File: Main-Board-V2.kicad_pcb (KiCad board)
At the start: 4 copper layers, 350 x 60 mm, 58 parts, among them IC1 REG1117-5, J2 776280-1, J3 776280-1, J4 1-776231-4, K1 J107F1AS123VDC.36, K2 J107F1AS123VDC.36, K3 J107F1AS123VDC.36, Q1 2N2222A, Q2 2N2222A, Q3 2N2222A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

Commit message: Moved CAN Ports to same side of board
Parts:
- moved C3 234.4 mm to (333.0, 105.7), turned to 180 degrees
- moved IC1 228.1 mm to (332.0, 112.0), turned to -90 degrees
- moved C2 224.5 mm to (326.1, 112.3)
- moved J3 69.8 mm to (130.8, 70.3), turned to 180 degrees
- moved U2 35.4 mm to (102.5, 97.0)
- moved C9 20.0 mm to (72.3, 110.1), turned to 180 degrees
- moved U3 19.9 mm to (71.5, 88.0), turned to 90 degrees
- moved C8 19.4 mm to (78.4, 102.4), turned to 90 degrees
- moved C4 18.0 mm to (71.6, 93.1), turned to 180 degrees
- moved C5 14.1 mm to (77.4, 85.7), turned to 90 degrees
- moved U12 11.2 mm to (72.5, 105.0), turned to 90 degrees
- moved J2 0.19 mm to (74.5, 70.3)
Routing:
- net /Can_RX1: track 108.6 -> 37.1 mm, vias 1 -> 0
- net /Can_TX1: track 128.5 -> 63.0 mm, vias 1 -> 0
- net +5V: track 361.7 -> 416.1 mm, vias 4 -> 2
- net +12V: track 291.9 -> 250.2 mm, vias 0 -> 2
- net /BattRelay: track 198.3 -> 233.1 mm
- net /USART_RX: track 116.8 -> 151.6 mm
- net /RightSignalIO: track 167.9 -> 202.7 mm
- net /Pedal/ThrottleIO: track 158.3 -> 193.1 mm
- net /Dio5: track 91.6 -> 126.4 mm
- net /Dio2: track 59.3 -> 94.1 mm
- net /ErrorIO: track 32.2 -> 67.0 mm
- net /Dio3: track 46.6 -> 81.4 mm
- net /USART_TX: track 119.4 -> 154.2 mm
- net /Pedal/BrakeIO: track 135.3 -> 170.1 mm
- net /LeftSignalIO: track 182.9 -> 217.7 mm
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
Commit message: Finalized analog components. Everything is done 🙏
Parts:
- removed R28, R29: R_US, Resistor_SMD:R_0805_2012Metric
- added C1: 1N, Capacitor_SMD:C_0805_2012Metric, F.Cu at (239.3, 107.1)
- added C6: 1N, Capacitor_SMD:C_0805_2012Metric, F.Cu at (255.0, 107.4)
- added C7: 1N, Capacitor_SMD:C_0805_2012Metric, F.Cu at (273.4, 109.5)
- added R6: 100R, Resistor_SMD:R_0805_2012Metric, F.Cu at (271.4, 98.3)
- added R7: 10k, Resistor_SMD:R_0805_2012Metric, F.Cu at (277.5, 99.3)
- C2, C3: footprint Cap10U:CAPC2012X145N -> Capacitor_SMD:C_0805_2012Metric
- R1, R20: value R_US -> 100R
- R2, R21, R22, R23, R24, R26, R3, R4: value R_US -> 10k
- R25, R27, R5: value R_US -> 1k
- moved R27 25.9 mm to (249.4, 107.4), turned to 0 degrees
- moved R25 11.6 mm to (268.8, 108.5)
- moved R26 9.57 mm to (249.4, 102.3), turned to 0 degrees
- moved R23 9.51 mm to (266.8, 103.4), turned to 0 degrees
- moved R22 9.38 mm to (260.6, 98.8), turned to -90 degrees
- moved R1 7.23 mm to (237.2, 96.9), turned to -90 degrees
- moved R3 6.90 mm to (243.3, 103.0)
- moved R21 6.73 mm to (277.5, 104.9), turned to 180 degrees
- moved R4 6.56 mm to (233.2, 102.0), turned to 0 degrees
- moved R2 6.34 mm to (243.8, 97.9), turned to -90 degrees
- moved U1 5.51 mm to (238.2, 101.5), turned to 90 degrees
- moved R20 4.62 mm to (254.0, 97.3), turned to -90 degrees
- moved R24 3.18 mm to (260.6, 103.9)
- moved U10 3.03 mm to (255.0, 102.3), turned to 90 degrees
- moved C3 2.93 mm to (334.4, 103.1)
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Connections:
- R21 pad 1: /Pedal/Throttle+ -> GND
- R21 pad 2: GND -> Net-(U11-+IN)
- R23 pad 1: /Pedal/Throttle+ -> GND
- R23 pad 2: Net-(U11-+IN) -> Net-(U11-OUT)
- R25 pad 1: GND -> Net-(U11-OUT)
- R25 pad 2: Net-(U11-+IN) -> /Pedal/ThrottleIO
- R27 pad 1: GND -> Net-(U10-OUT)
- R27 pad 2: Net-(U11-OUT) -> /Pedal/BrakeIO
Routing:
- net +12V: track 250.2 -> 277.5 mm, vias 2 -> 1
- net /EncoderIO: track 141.6 -> 151.5 mm
- net /Pedal/Brake+: track 33.6 -> 26.7 mm
- net /Pedal/ThrottleIO: track 193.1 -> 188.1 mm
- net /Encoder: track 30.8 -> 25.9 mm
- net Net-(U10-OUT): track 5.20 -> 10.1 mm
- net GND: track 142.3 -> 139.5 mm, vias 20 -> 15
- net Net-(U11-OUT): track 6.29 -> 8.81 mm
- net Net-(U11-+IN): track 6.39 -> 8.89 mm
- net /Pedal/BrakeIO: track 170.1 -> 168.0 mm
- net Net-(U10-+IN): track 6.30 -> 8.38 mm
- net +5V: track 416.1 -> 414.4 mm
- net +3.3V: track 217.2 -> 218.8 mm, vias 4 -> 8
- net Net-(U1-OUT): track 8.80 -> 9.93 mm
- net /Pedal/Throttle+: track 34.2 -> 33.5 mm
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
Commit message: Added fuse, switch to horizontal connecotor, redid all routing
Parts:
- added F1: Fuse, Fuse:Fuse_0805_2012Metric, F.Cu at (187.5, 81.5)
- J4: value 1-776231-4 -> 1-776163-5; footprint 1-776231-4:TE_1-776231-4 -> 776163-5:TE_776163-5
- moved K2 258.1 mm to (57.5, 98.0)
- moved Q2 258.1 mm to (57.5, 110.7)
- moved R30 258.1 mm to (58.1, 85.3)
- moved K1 244.7 mm to (85.5, 98.0)
- moved Q1 244.7 mm to (85.9, 110.8)
- moved K3 229.1 mm to (71.9, 98.0)
- moved Q3 229.1 mm to (71.9, 110.7)
- moved R31 229.1 mm to (71.3, 85.9)
- moved R7 176.8 mm to (101.0, 111.1)
- moved R6 175.3 mm to (96.5, 111.1)
- moved R21 171.6 mm to (106.0, 111.1), turned to -90 degrees
- moved U11 170.4 mm to (102.0, 117.1), turned to -90 degrees
- moved R23 159.8 mm to (107.5, 116.6), turned to 90 degrees
- moved R25 156.5 mm to (112.5, 116.6), turned to -90 degrees
- moved C7 156.0 mm to (117.5, 116.6)
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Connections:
- J2 pad 1: +12V -> Net-(F1-Pad1)
- J3 pad 1: +12V -> Net-(F1-Pad1)
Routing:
- net +5V: track 414.4 -> 212.5 mm, vias 2 -> 3
- net /Pedal/ThrottleIO: track 188.1 -> 5.02 mm, vias 1 -> 0
- net /Pedal/BrakeIO: track 168.0 -> 4.76 mm, vias 1 -> 0
- net /USART_TX: track 154.2 -> 0.00 mm
- net /USART_RX: track 151.6 -> 0.00 mm
- net /EncoderIO: track 151.5 -> 0.00 mm, vias 1 -> 0
- net /BattRelay: track 233.1 -> 93.7 mm
- net /RightSignalIO: track 202.4 -> 108.1 mm
- net /LeftSignalIO: track 217.7 -> 123.9 mm
- net /Pedal/Error: track 95.9 -> 12.3 mm
- net /Dio1: track 106.5 -> 32.2 mm
- net /Dio4: track 116.0 -> 50.5 mm
- net GND: track 139.5 -> 74.1 mm, vias 15 -> 8
- net /Dio5: track 126.4 -> 69.4 mm
- net /DigitalInputs/Button3: track 73.7 -> 17.5 mm
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- removed copper zone on In2.Cu, net +12V
- removed copper zone on In2.Cu, net +3.3V
- removed copper zone on B.Cu, net GND
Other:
- board size 350 x 60 mm -> 201 x 70.1 mm
- copper layers 4 -> 2

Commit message: finished re-routing, only silkscreen errors left
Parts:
- moved R3 71.6 mm to (143.5, 117.5), turned to 0 degrees
- moved R2 66.8 mm to (143.5, 112.5)
- moved U1 64.7 mm to (148.5, 113.0), turned to -90 degrees
- moved R1 62.6 mm to (143.5, 108.0), turned to 0 degrees
- moved R4 62.2 mm to (153.0, 117.0), turned to 180 degrees
- moved G*** 57.8 mm to (142.0, 96.5)
- moved R5 57.0 mm to (153.0, 112.5), turned to 0 degrees
- moved C1 53.5 mm to (153.0, 108.0), turned to 180 degrees
- moved R21 12.3 mm to (95.5, 117.5), turned to 0 degrees
- moved C7 11.6 mm to (106.0, 117.5), turned to 180 degrees
- moved R24 11.0 mm to (114.0, 117.5), turned to 0 degrees
- moved R20 8.73 mm to (114.0, 108.5), turned to 0 degrees
- moved U10 8.73 mm to (119.5, 113.0)
- moved R26 8.38 mm to (124.5, 108.5), turned to 180 degrees
- moved R23 8.23 mm to (106.0, 108.5), turned to 180 degrees
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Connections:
- C6 pad 1: /Pedal/BrakeIO -> /BrakeIO
- C7 pad 1: /Pedal/ThrottleIO -> /ThrottleIO
- R25 pad 2: /Pedal/ThrottleIO -> /ThrottleIO
- R27 pad 2: /Pedal/BrakeIO -> /BrakeIO
- U2 pad 10: /Dio2 -> unconnected-(U2-8_TX2_IN1-Pad10)
- U2 pad 11: /Dio3 -> unconnected-(U2-9_OUT1C-Pad11)
- U2 pad 12: /ErrorIO -> /BattRelay
- U2 pad 13: unconnected-(U2-11_MOSI_CTX1-Pad13) -> /RightSignalIO
- U2 pad 14: unconnected-(U2-12_MISO_MQSL-Pad14) -> /LeftSignalIO
- U2 pad 23: /USART_RX -> /ThrottleIO
- U2 pad 24: /USART_TX -> /BrakeIO
- U2 pad 25: unconnected-(U2-18_A4_SDA0-Pad25) -> /EncoderIO
- U2 pad 26: /EncoderIO -> unconnected-(U2-19_A5_SCL0-Pad26)
- U2 pad 27: /Pedal/BrakeIO -> /USART_TX
- U2 pad 28: /Pedal/ThrottleIO -> /USART_RX
- U2 pad 4: /BattRelay -> /Dio1
- U2 pad 5: /LeftSignalIO -> /Dio2
- U2 pad 6: /RightSignalIO -> /Dio3
- U2 pad 7: /Dio5 -> /Dio4
- U2 pad 8: /Dio4 -> /Dio5
- U2 pad 9: /Dio1 -> /ErrorIO
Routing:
- net /USART_TX: track 0.00 -> 106.2 mm, vias 0 -> 1
- net /USART_RX: track 0.00 -> 97.8 mm, vias 0 -> 1
- net /ThrottleIO: track 0.00 -> 91.6 mm, vias 0 -> 1
- net /BrakeIO: track 0.00 -> 73.0 mm, vias 0 -> 1
- net /Encoder: track 0.00 -> 72.0 mm
- net +3.3V: track 198.9 -> 257.8 mm, vias 7 -> 9
- net /Pedal/Brake+: track 48.8 -> 4.50 mm
- net /EncoderIO: track 0.00 -> 42.7 mm, vias 0 -> 1
- net GND: track 74.1 -> 111.6 mm, vias 8 -> 16
- net /Pedal/Throttle+: track 37.1 -> 4.50 mm
- net /Dio4: track 50.5 -> 60.1 mm, vias 0 -> 1
- net Net-(U1-+IN): track 0.00 -> 8.45 mm
- net Net-(U1-OUT): track 0.00 -> 7.45 mm
- net /Pedal/ThrottleIO: track 5.02 -> 0.00 mm
- net /Pedal/BrakeIO: track 4.76 -> 0.00 mm
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- added copper zone on B.Cu, net GND
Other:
- board text added: "${REFERENCE}"
- board text removed: "1"
- board text removed: "10"
- board text removed: "11"
- board text removed: "12"
- board text removed: "13"
- board text removed: "14"
- board text removed: "15"
- board text removed: "16"
- board text removed: "17"
- board text removed: "18"
- board text removed: "19"
- board text removed: "2"
- board text removed: "20"
- board text removed: "21"
- board text removed: "22"
- board text removed: "23"
- board text removed: "24"
- board text removed: "25"
- board text removed: "26"
- board text removed: "27"
- board text removed: "28"
- board text removed: "29"
- board text removed: "3"
- board text removed: "30"
- board text removed: "31"
- board text removed: "32"
- board text removed: "33"
- board text removed: "34"
- board text removed: "4"
- board text removed: "5"
- board text removed: "6"
- board text removed: "7"
- board text removed: "8"
- board text removed: "9"

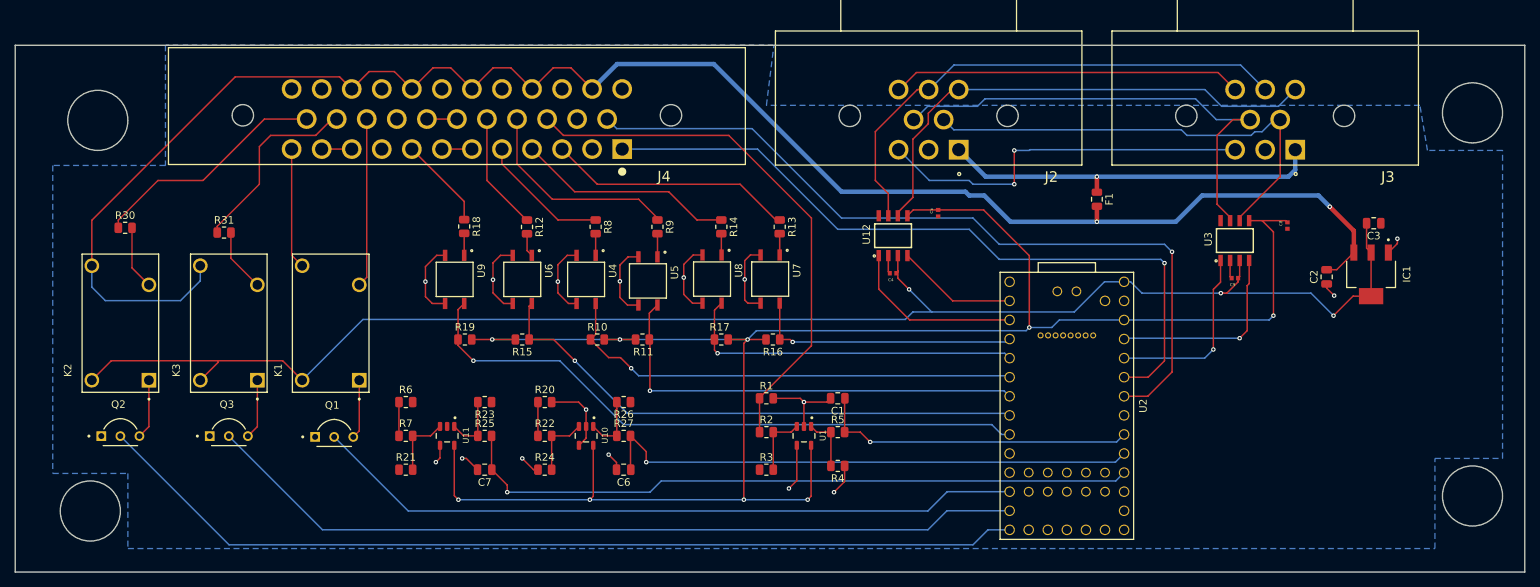
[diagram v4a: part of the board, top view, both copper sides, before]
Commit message: fixed silk screen
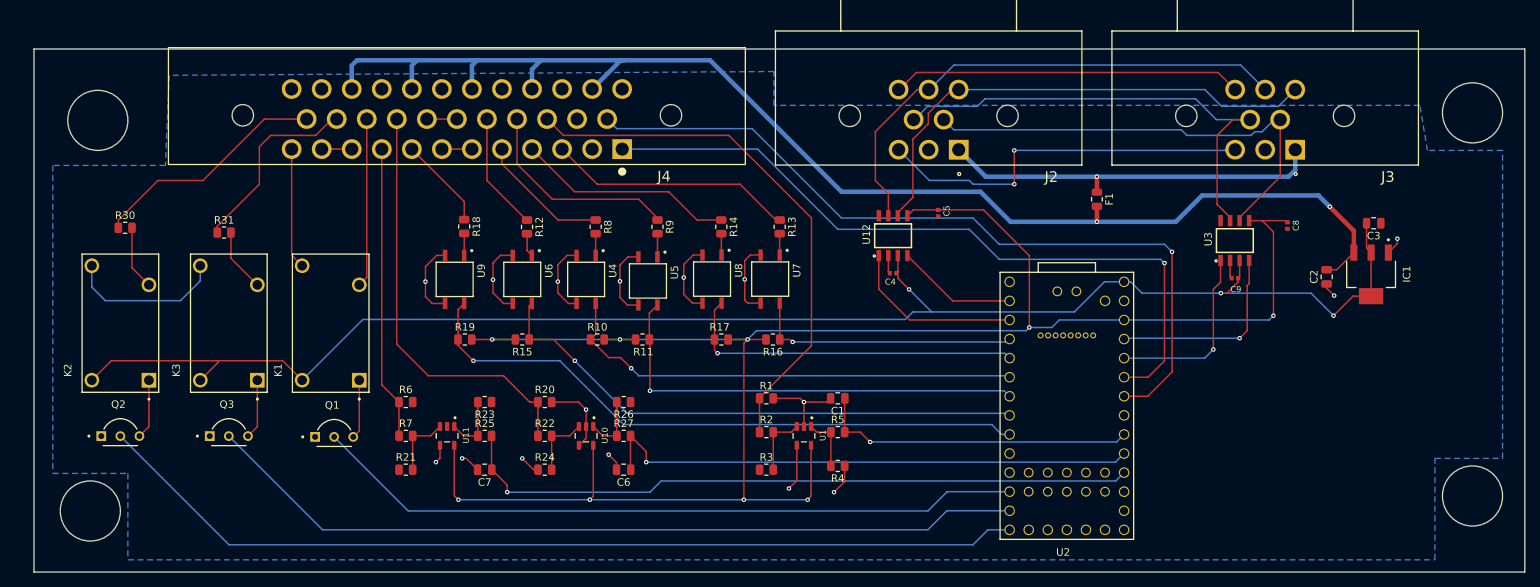
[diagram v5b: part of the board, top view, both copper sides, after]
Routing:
- net /Pedal/Brake+: track 4.50 -> 56.5 mm
- net +12V: track 235.7 -> 198.1 mm
- net /Pedal/Throttle+: track 4.50 -> 39.1 mm
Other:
- board size 201 x 70.1 mm -> 198.5 x 69.6 mm
- board text added: "Teensy4.0"
- board text removed: "${REFERENCE}"

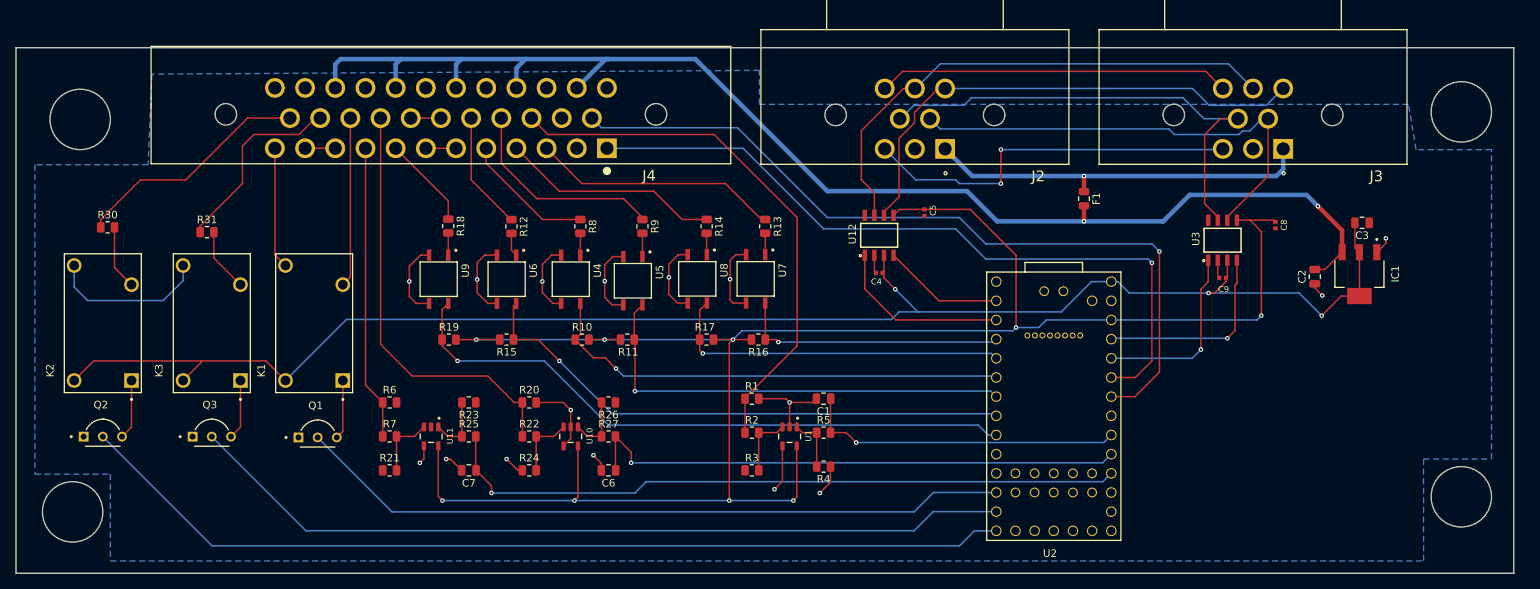
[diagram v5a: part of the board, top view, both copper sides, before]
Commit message: added LED indicators, fixed footprints
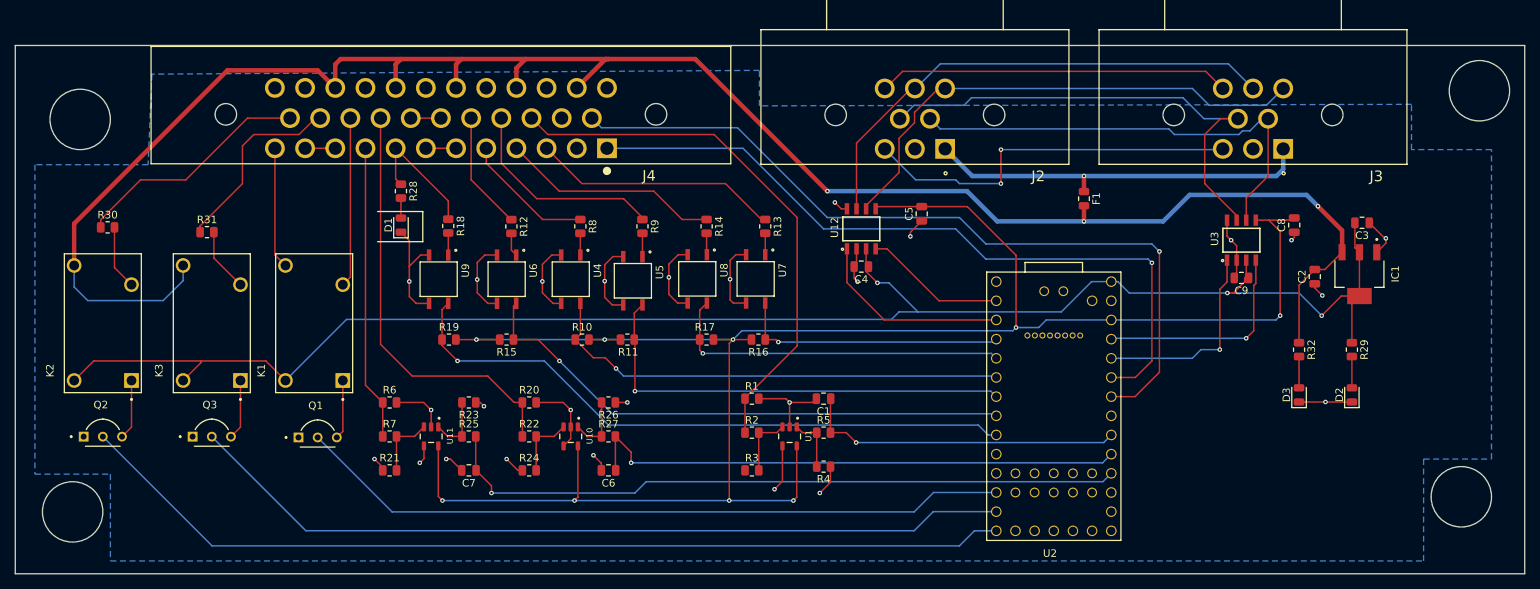
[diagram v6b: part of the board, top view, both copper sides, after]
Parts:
- added D1: LED, LED_SMD:LED_0805_2012Metric, F.Cu at (97.0, 85.0)
- added D2: LED, LED_SMD:LED_0805_2012Metric, F.Cu at (223.0, 107.5)
- added D3: LED, LED_SMD:LED_0805_2012Metric, F.Cu at (216.0, 107.5)
- added R28: R_US, Resistor_SMD:R_0805_2012Metric, F.Cu at (97.0, 80.5)
- added R29: R_US, Resistor_SMD:R_0805_2012Metric, F.Cu at (223.0, 101.5)
- added R32: R_US, Resistor_SMD:R_0805_2012Metric, F.Cu at (216.0, 101.5)
- C4, C5, C8, C9: footprint GRT155C80J105KE01J:CAPC1005X55N -> Capacitor_SMD:C_0805_2012Metric
- moved C4 2.51 mm to (158.0, 90.5)
- moved U12 2.51 mm to (158.0, 85.5)
- moved C8 2.50 mm to (215.3, 85.0)
- moved C9 2.50 mm to (208.3, 92.0)
- moved U3 2.50 mm to (208.3, 87.0)
- moved C5 0.39 mm to (166.0, 83.5)
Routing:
- net +12V: track 198.1 -> 258.2 mm, vias 2 -> 3
- net GND: track 111.6 -> 152.0 mm, vias 16 -> 26
- net +5V: track 210.0 -> 219.0 mm
- net /Pedal/Error: track 12.3 -> 17.3 mm
- net +3.3V: track 257.8 -> 262.3 mm
- net Net-(D3-A): track 0.00 -> 4.15 mm
- net Net-(D2-A): track 0.00 -> 4.15 mm
- net /Can_TX1: track 23.6 -> 26.3 mm
- net /Can_RX1: track 16.1 -> 18.8 mm
- net Net-(D1-A): track 0.00 -> 2.65 mm
- net /Can/CanTx0: track 24.6 -> 27.1 mm
- net /Can/CanRx0: track 26.3 -> 28.8 mm
- net /Can/CaNH1: track 68.7 -> 66.9 mm
- net /Can/CaNL0: track 62.2 -> 61.2 mm
- net /Can/CaNH0: track 64.3 -> 65.4 mm
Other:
- board size 198.5 x 69.6 mm -> 200 x 70 mm
